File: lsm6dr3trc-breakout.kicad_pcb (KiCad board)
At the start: 2 copper layers, 15.2 x 20.6 mm, 15 parts, among them CN1 AFC10-S04QCA-00, CN2 AFC10-S04QCA-00, J1 Conn_01x06_Pin, J2 Conn_01x04_Pin, U1 LSM6DS3TR-C

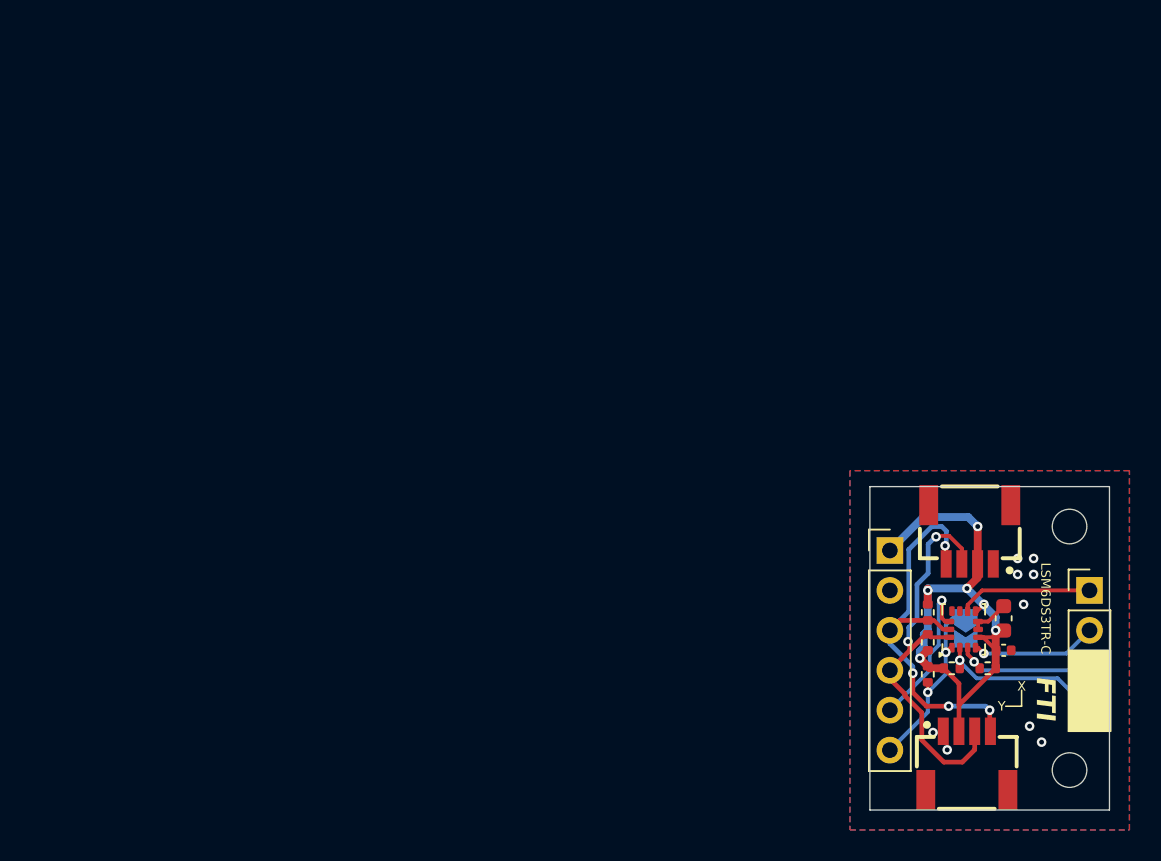
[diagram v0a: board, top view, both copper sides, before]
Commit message: unified IMU footprint
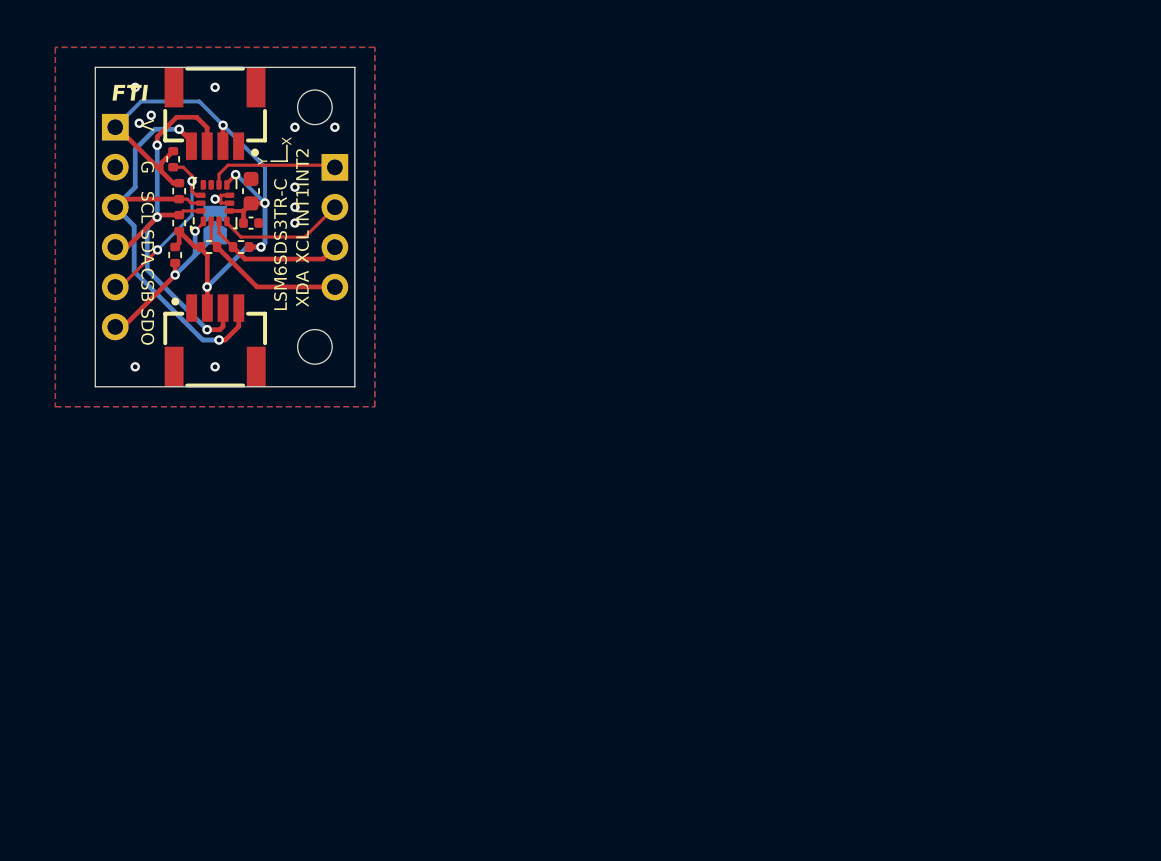
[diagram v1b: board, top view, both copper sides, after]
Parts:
- removed the R1 at (107.8, 78.6)
- added R1: 2.2k, Resistor_SMD:R_0402_1005Metric, F.Cu at (56.0, 46.2)
- added R1: 3.9k, Resistor_SMD:R_0402_1005Metric, F.Cu at (60.3, 51.8)
- CN1, CN2: footprint lsm6dr3trc-breakout:CONN-SMD_AFC10-S04QCA-00 -> qwiic:CONN-SMD_AFC10-S04QCA-00
- moved H1 63.9 mm to (65.0, 42.9)
- moved J1 56.2 mm to (52.3, 44.2)
- moved C1 55.1 mm to (61.0, 48.3)
- moved C2 55.1 mm to (61.0, 50.3)
- moved J2 55.0 mm to (66.3, 46.7)
- moved CN1 54.9 mm to (58.7, 43.5)
- moved CN2 54.9 mm to (58.7, 57.6)
- moved R5 54.8 mm to (56.1, 52.3)
- moved U1 54.8 mm to (58.7, 49.0)
- moved R4 54.6 mm to (56.4, 48.3)
- moved R3 54.6 mm to (56.4, 50.3)
- moved R2 54.3 mm to (58.3, 51.8)
- moved JP1 54.2 mm to (58.7, 50.4), turned to 90 degrees
- moved H2 49.3 mm to (65.0, 58.2)
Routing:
- net VDD: track 39.6 -> 45.6 mm, vias 6 -> 5
- net /SCL: track 26.5 -> 29.2 mm, vias 4 -> 2
- net /CS: track 10.1 -> 11.9 mm, vias 1 -> 2
- net /SDA: track 26.5 -> 28.4 mm, vias 2 -> 3
- net /XDA: track 10.8 -> 10.2 mm, vias 1 -> 0
- net GND: track 2.53 -> 2.99 mm, vias 9 -> 12
- net /XCL: track 9.12 -> 9.01 mm, vias 1 -> 0
- net /INT1: track 8.02 -> 8.03 mm, vias 1 -> 0
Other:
- board size 15.2 x 20.6 mm -> 16.5 x 20.3 mm
- board text added: "CSB"
- board text added: "G"
- board text added: "LSM6SDS3TR-C"
- board text added: "V"
- board text removed: "3V3"
- board text removed: "ADDR 0x6B DEFAULT 0x6A JUMPER"
- board text removed: "CS"
- board text removed: "LSM6DS3TR-C"

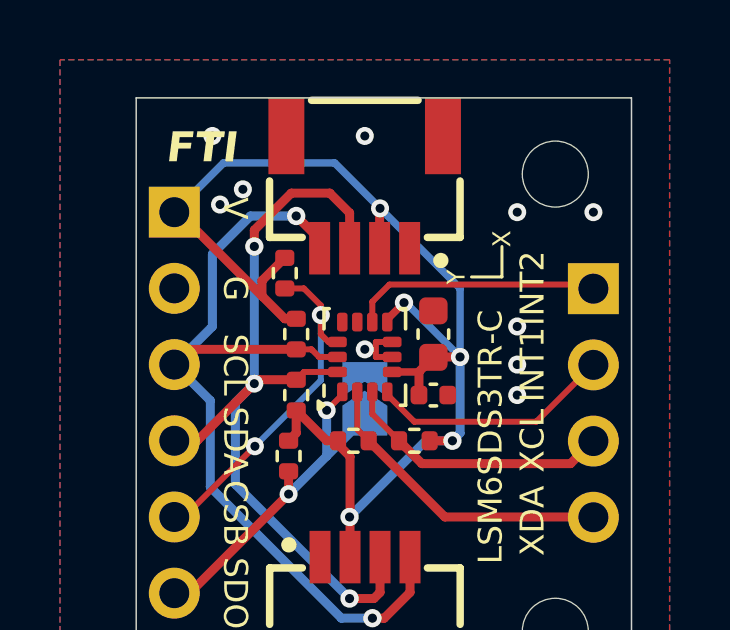
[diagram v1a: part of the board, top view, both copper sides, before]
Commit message: fix csb resistor, beautify schematic
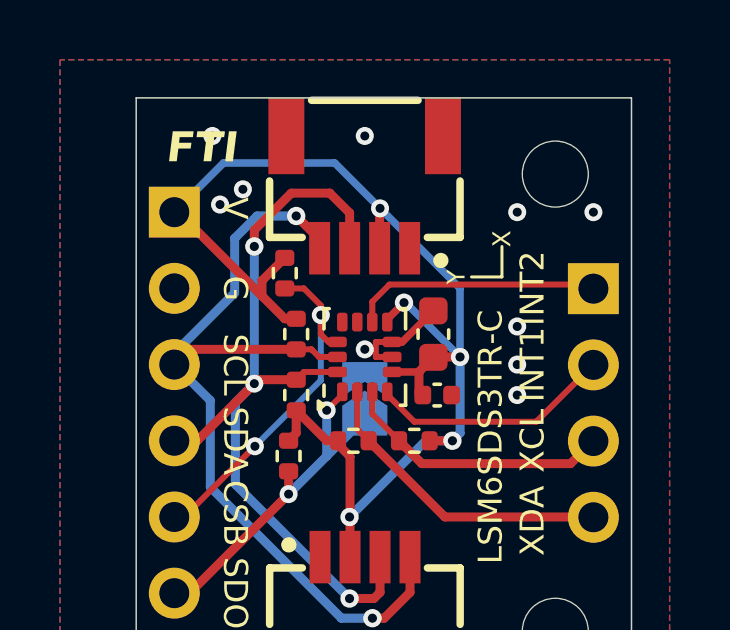
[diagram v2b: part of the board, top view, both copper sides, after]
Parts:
- removed the R1 at (56.0, 46.2)
- removed the R1 at (60.3, 51.8)
- added R1: 2.2k, Resistor_SMD:R_0402_1005Metric, F.Cu at (56.4, 48.3)
- added R6: 2.2k, Resistor_SMD:R_0402_1005Metric, F.Cu at (56.0, 46.2)
- R2, R3, R4, R5: value 3.9k -> 2.2k
- moved R3 4.22 mm to (60.3, 51.8), turned to 180 degrees
- moved R4 4.03 mm to (58.3, 51.8), turned to 0 degrees
- moved R2 2.44 mm to (56.4, 50.3), turned to 90 degrees
- moved C2 0.13 mm to (61.1, 50.3)
- turned C1 to 90 degrees
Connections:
- C1 pad 1: GND -> VDD
- C1 pad 2: VDD -> GND
- R2 pad 2: /XDA -> /SDA
- R3 pad 1: /SDA -> VDD
- R3 pad 2: VDD -> /XCL
- R4 pad 1: /SCL -> VDD
- R4 pad 2: VDD -> /XDA
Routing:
- net GND: track 2.99 -> 4.50 mm

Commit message: use lower pullups
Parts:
- R1, R2, R3, R4, R5, R6: value 2.2k -> 4.7k
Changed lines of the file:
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@@
 				(font
 					(size 1.27 1.27)
+					(thickness 0.15)
 				)
 			)
@@
 				(font
 					(size 1.27 1.27)
+					(thickness 0.15)
 				)
 			)
@@
 				(font
 					(size 1.27 1.27)
+					(thickness 0.15)
 				)
 			)
@@
 			)
 		)
-		(property "Value" "2.2k"
+		(property "Value" "4.7k"
 			(at 0 1.17 -90)
 			(layer "F.Fab")
@@
 				(font
 					(size 1.27 1.27)
+					(thickness 0.15)
 				)
 			)
@@
 				(font
 					(size 1.27 1.27)
+					(thickness 0.15)
 				)
 			)
@@
 				(font
 					(size 1.27 1.27)
+					(thickness 0.15)
 				)
 			)
@@
 				(font
 					(size 1.27 1.27)
+					(thickness 0.15)
 				)
 			)
@@
 				(font
 					(size 1.27 1.27)
+					(thickness 0.15)
 				)
 			)
@@
 				(font
 					(size 1.27 1.27)
+					(thickness 0.15)
 				)
 			)
@@
 				(font
 					(size 1.27 1.27)
+					(thickness 0.15)
 				)
 			)
@@
 				(font
 					(size 1.27 1.27)
+					(thickness 0.15)
 				)
 			)
@@
 				(font
 					(size 1.27 1.27)
+					(thickness 0.15)
 				)
 			)
@@
 				(font
 					(size 1.27 1.27)
+					(thickness 0.15)
 				)
 			)
@@
 				(font
 					(size 1.27 1.27)
+					(thickness 0.15)
 				)
 			)
@@
 				(font
 					(size 1.27 1.27)
+					(thickness 0.15)
 				)
 			)
@@
 			)
 		)
-		(property "Value" "2.2k"
+		(property "Value" "4.7k"
 			(at 0 1.17 90)
 			(layer "F.Fab")
@@
 				(font
 					(size 1.27 1.27)
+					(thickness 0.15)
 				)
 			)
@@
 				(font
 					(size 1.27 1.27)
+					(thickness 0.15)
 				)
 			)
@@
 				(font
 					(size 1.27 1.27)
+					(thickness 0.15)
 				)
 			)
@@
 				(font
 					(size 1.27 1.27)
+					(thickness 0.15)
 				)
 			)
@@
 				(font
 					(size 1.27 1.27)
+					(thickness 0.15)
 				)
 			)
@@
 				(font
 					(size 1.27 1.27)
+					(thickness 0.15)
 				)
 			)
@@
 				(font
 					(size 1.27 1.27)
+					(thickness 0.15)
 				)
 			)
@@
 				(font
 					(size 1.27 1.27)
+					(thickness 0.15)
 				)
 			)
@@
 				(font
 					(size 1.27 1.27)
+					(thickness 0.15)
 				)
 			)
@@
 			)
 		)
-		(property "Value" "2.2k"
+		(property "Value" "4.7k"
 			(at 0 1.17 90)
 			(layer "F.Fab")
@@
 				(font
 					(size 1.27 1.27)
+					(thickness 0.15)
 				)
 			)
@@
 				(font
 					(size 1.27 1.27)
+					(thickness 0.15)
 				)
 			)
@@
 				(font
 					(size 1.27 1.27)
+					(thickness 0.15)
 				)
 			)
@@
 			)
 		)
-		(property "Value" "2.2k"
+		(property "Value" "4.7k"
 			(at 0 1.17 90)
 			(layer "F.Fab")
@@
 				(font
 					(size 1.27 1.27)
+					(thickness 0.15)
 				)
 			)
@@
 				(font
 					(size 1.27 1.27)
+					(thickness 0.15)
 				)
 			)
@@
 				(font
 					(size 1.27 1.27)
+					(thickness 0.15)
 				)
 			)
@@
 				(font
 					(size 1.27 1.27)
+					(thickness 0.15)
 				)
 			)
@@
 				(font
 					(size 1.27 1.27)
+					(thickness 0.15)
 				)
 			)
@@
 				(font
 					(size 1.27 1.27)
+					(thickness 0.15)
 				)
 			)
@@
 				(font
 					(size 1.27 1.27)
+					(thickness 0.15)
 				)
 			)
@@
 				(font
 					(size 1.27 1.27)
+					(thickness 0.15)
 				)
 			)
@@
 				(font
 					(size 1.27 1.27)
+					(thickness 0.15)
 				)
 			)
@@
 			)
 		)
-		(property "Value" "2.2k"
+		(property "Value" "4.7k"
 			(at 0 1.17 180)
 			(layer "F.Fab")
@@
 				(font
 					(size 1.27 1.27)
+					(thickness 0.15)
 				)
 			)
@@
 				(font
 					(size 1.27 1.27)
+					(thickness 0.15)
 				)
 			)
@@
 				(font
 					(size 1.27 1.27)
+					(thickness 0.15)
 				)
 			)
@@
 				(font
 					(size 1.27 1.27)
+					(thickness 0.15)
 				)
 			)
@@
 				(font
 					(size 1.27 1.27)
+					(thickness 0.15)
 				)
 			)
@@
 				(font
 					(size 1.27 1.27)
+					(thickness 0.15)
 				)
 			)
@@
 			)
 		)
-		(property "Value" "2.2k"
+		(property "Value" "4.7k"
 			(at 0 1.17 0)
 			(layer "F.Fab")
@@
 				(font
 					(size 1.27 1.27)
+					(thickness 0.15)
 				)
 			)
@@
 				(font
 					(size 1.27 1.27)
+					(thickness 0.15)
 				)
 			)
@@
 				(font
 					(size 1.27 1.27)
+					(thickness 0.15)
 				)
 			)
@@
 				(font
 					(size 1.27 1.27)
+					(thickness 0.15)
 				)
 				(justify mirror)
@@
 				(font
 					(size 1.27 1.27)
+					(thickness 0.15)
 				)
 				(justify mirror)
@@
 				(font
 					(size 1.27 1.27)
+					(thickness 0.15)
 				)
 				(justify mirror)

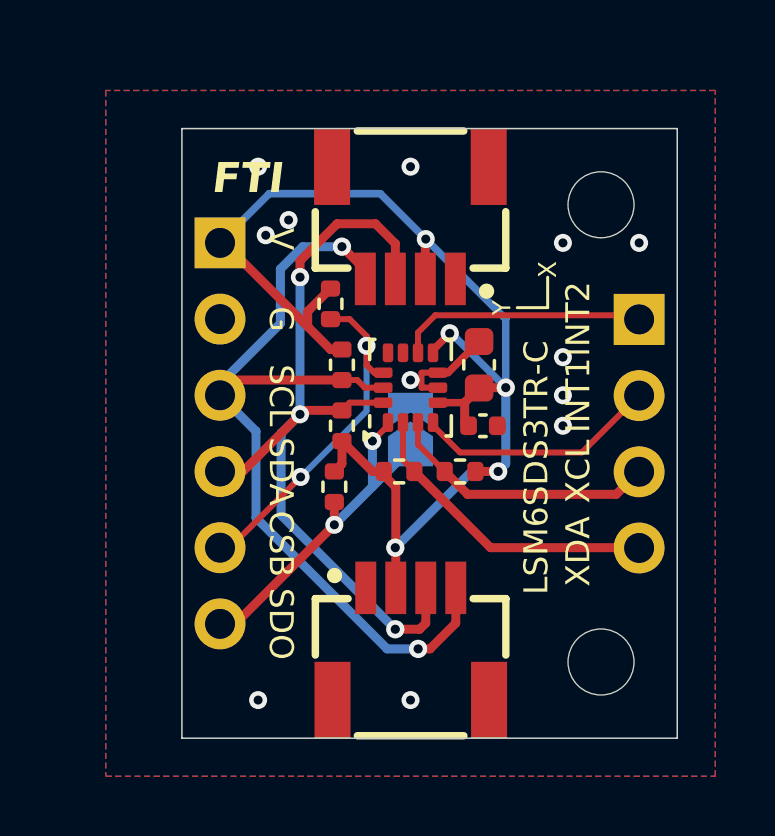
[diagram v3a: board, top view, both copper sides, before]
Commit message: make it dipable
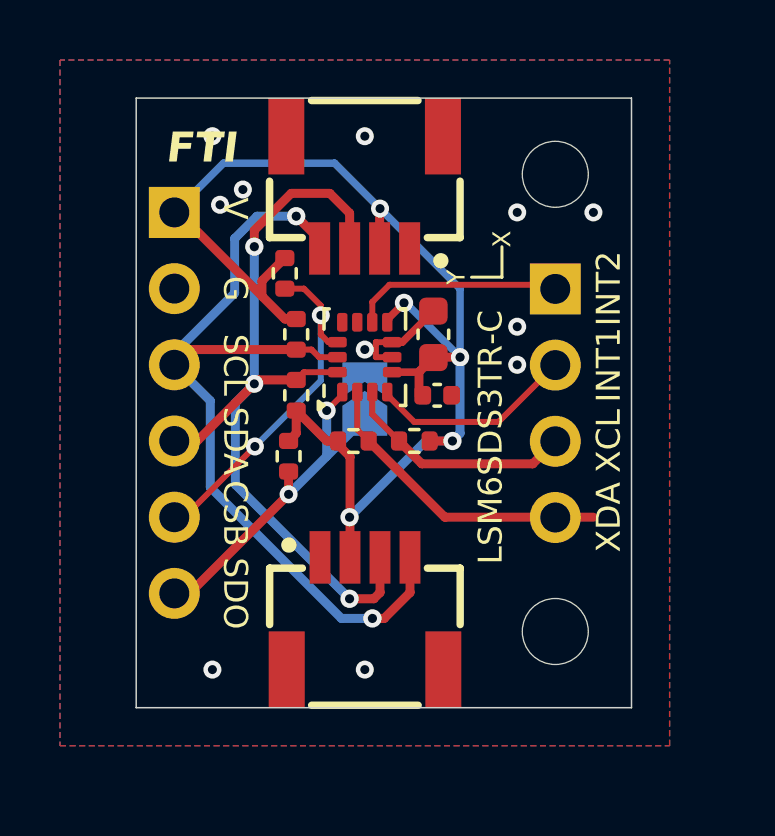
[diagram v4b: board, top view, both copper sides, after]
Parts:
- moved J2 2.97 mm to (63.5, 45.7)
- moved H1 1.83 mm to (63.5, 41.9)
- moved R3 1.83 mm to (58.8, 50.8)
- moved R4 1.83 mm to (56.8, 50.8)
- moved C1 1.83 mm to (59.4, 47.2)
- moved C2 1.83 mm to (59.6, 49.3)
- moved CN2 1.83 mm to (57.2, 56.5)
- moved H2 1.83 mm to (63.5, 57.1)
- moved J1 1.83 mm to (50.8, 43.2)
- moved JP1 1.83 mm to (57.1, 49.4)
- moved R1 1.83 mm to (54.9, 47.2)
- moved R2 1.83 mm to (54.9, 49.3)
- moved R5 1.83 mm to (54.6, 51.3)
- moved R6 1.83 mm to (54.5, 45.2)
- moved U1 1.83 mm to (57.1, 48.0)
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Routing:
- net /INT1: track 8.03 -> 6.76 mm
- net /INT2: track 8.24 -> 6.97 mm
- net /XCL: track 9.01 -> 7.75 mm
- net GND: vias 12 -> 11
